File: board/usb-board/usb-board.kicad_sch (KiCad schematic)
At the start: 34 parts, among them J1 USB_C_Receptacle_USB2.0_16P, J3 RS485, J4 Conn_01x04_Pin, SW1 SW_DIP_x03, U1 AMS1117-3.3, U2 STM32F103C8T6, U3 MAX485E, Y1 8Mhz

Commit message: [ENH] Enhance scheme board
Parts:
- added R13, R14: 20, Resistor_SMD:R_1206_3216Metric_Pad1.30x1.75mm_HandSolder, symbol Device:R
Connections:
- net +3.3VA is gone; now on net +3.3V: U2.1 (VBAT), U2.24 (VDD), U2.36 (VDD), U2.48 (VDD), U2.9 (VDDA)
- net +3V3 is gone; now on net +3.3V: R12.1, U3.8 (VCC)
- net USB_D+: now also R13.1; no longer J1.A6 (D+), J1.B6 (D+)
- net USB_D-: now also R14.1; no longer J1.A7 (D-), J1.B7 (D-)
- new net: J1.A7 (D-), J1.B7 (D-), R14.2
- new net: J1.A6 (D+), J1.B6 (D+), R13.2
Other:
- moved on the sheet: R5
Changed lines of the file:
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@@
 	)
 	(junction
-		(at 213.36 86.36)
-		(diameter 0)
-		(color 0 0 0 0)
-	)
-	(junction
 		(at 240.03 147.32)
 		(diameter 0)
@@
 	)
 	(junction
+		(at 209.55 86.36)
+		(diameter 0)
+		(color 0 0 0 0)
+	)
+	(junction
 		(at 187.96 46.99)
 		(diameter 0)
@@
 	(wire
 		(pts
-			(xy 213.36 86.36) (xy 229.87 86.36)
-		)
-		(stroke
-			(width 0)
-			(type default)
-		)
-	)
-	(wire
-		(pts
 			(xy 157.48 83.82) (xy 165.1 83.82)
 		)
@@
 	(wire
 		(pts
-			(xy 213.36 86.36) (xy 198.12 86.36)
+			(xy 218.44 86.36) (xy 229.87 86.36)
 		)
 		(stroke
@@
 	(wire
 		(pts
-			(xy 213.36 82.55) (xy 213.36 86.36)
+			(xy 209.55 86.36) (xy 210.82 86.36)
+		)
+		(stroke
+			(width 0)
+			(type default)
+		)
+	)
+	(wire
+		(pts
+			(xy 209.55 82.55) (xy 209.55 86.36)
 		)
 		(stroke
@@
 	(wire
 		(pts
-			(xy 198.12 83.82) (xy 240.03 83.82)
+			(xy 198.12 83.82) (xy 219.71 83.82)
 		)
 		(stroke
@@
 	(wire
 		(pts
-			(xy 213.36 72.39) (xy 213.36 74.93)
-		)
-		(stroke
-			(width 0)
-			(type default)
-		)
-	)
-	(wire
-		(pts
 			(xy 74.93 96.52) (xy 82.55 96.52)
 		)
@@
 	(wire
 		(pts
+			(xy 227.33 83.82) (xy 240.03 83.82)
+		)
+		(stroke
+			(width 0)
+			(type default)
+		)
+	)
+	(wire
+		(pts
 			(xy 198.12 78.74) (xy 200.66 78.74)
 		)
@@
 	(wire
 		(pts
+			(xy 198.12 86.36) (xy 209.55 86.36)
+		)
+		(stroke
+			(width 0)
+			(type default)
+		)
+	)
+	(wire
+		(pts
 			(xy 60.96 39.37) (xy 60.96 41.91)
 		)
@@
 			)
 		)
-		(property "Value" "+3.3VA"
-			(at 187.96 25.4 0)
+		(property "Value" "+3.3V"
+			(at 190.5 29.2099 0)
 			(effects
 				(font
 					(size 1.27 1.27)
 				)
+				(justify left)
 			)
 		)
@@
 	)
 	(symbol
+		(lib_id "Device:R")
+		(at 223.52 83.82 90)
+		(unit 1)
+		(exclude_from_sim no)
+		(in_bom yes)
+		(on_board yes)
+		(dnp no)
+		(fields_autoplaced yes)
+		(property "Reference" "R14"
+			(at 223.52 77.47 90)
+			(effects
+				(font
+					(size 1.27 1.27)
+				)
+			)
+		)
+		(property "Value" "20"
+			(at 223.52 80.01 90)
+			(effects
+				(font
+					(size 1.27 1.27)
+				)
+			)
+		)
+		(property "Footprint" "Resistor_SMD:R_1206_3216Metric_Pad1.30x1.75mm_HandSolder"
+			(at 223.52 85.598 90)
+			(effects
+				(font
+					(size 1.27 1.27)
+				)
+				(hide yes)
+			)
+		)
+		(property "Datasheet" "~"
+			(at 223.52 83.82 0)
+			(effects
+				(font
+					(size 1.27 1.27)
+				)
+				(hide yes)
+			)
+		)
+		(property "Description" ""
+			(at 223.52 83.82 0)
+			(effects
+				(font
+					(size 1.27 1.27)
+				)
+			)
+		)
+		(pin "1"
+		)
+		(pin "2"
+		)
+		(instances
+			(project "usb-board"
+				(path "/738c6582-c171-41c5-9c7c-967a52446e9f"
+					(reference "R14")
+					(unit 1)
+				)
+			)
+		)
+	)
+	(symbol
 		(lib_id "power:GND")
 		(at 21.59 153.67 0)
@@
 		(on_board yes)
 		(dnp no)
-		(fields_autoplaced yes)
 		(property "Reference" "#PWR08"
 			(at 57.15 80.01 0)
@@
 			)
 		)
-		(property "Value" "+3V3"
-			(at 57.15 71.12 0)
+		(property "Value" "+3.3V"
+			(at 56.134 70.866 0)
 			(effects
 				(font
 					(size 1.27 1.27)
 				)
+				(justify left)
 			)
 		)
@@
 	(symbol
 		(lib_id "Device:R")
-		(at 213.36 78.74 0)
+		(at 209.55 78.74 0)
 		(unit 1)
 		(exclude_from_sim no)
@@
 		(on_board yes)
 		(dnp no)
-		(fields_autoplaced yes)
 		(property "Reference" "R5"
-			(at 215.9 77.47 0)
+			(at 212.09 77.47 0)
 			(effects
 				(font
@@
 		)
 		(property "Value" "1K5"
-			(at 215.9 80.01 0)
+			(at 212.09 80.01 0)
 			(effects
 				(font
@@
 		)
 		(property "Footprint" "Resistor_SMD:R_1206_3216Metric_Pad1.30x1.75mm_HandSolder"
-			(at 211.582 78.74 90)
+			(at 207.772 78.74 90)
 			(effects
 				(font
@@
 		)
 		(property "Datasheet" "~"
-			(at 213.36 78.74 0)
+			(at 209.55 78.74 0)
 			(effects
 				(font
@@
 		)
 		(property "Description" ""
-			(at 213.36 78.74 0)
+			(at 209.55 78.74 0)
 			(effects
 				(font
@@
 	(symbol
 		(lib_id "Device:R")
+		(at 214.63 86.36 90)
+		(unit 1)
+		(exclude_from_sim no)
+		(in_bom yes)
+		(on_board yes)
+		(dnp no)
+		(property "Reference" "R13"
+			(at 214.63 90.424 90)
+			(effects
+				(font
+					(size 1.27 1.27)
+				)
+			)
+		)
+		(property "Value" "20"
+			(at 214.376 88.646 90)
+			(effects
+				(font
+					(size 1.27 1.27)
+				)
+			)
+		)
+		(property "Footprint" "Resistor_SMD:R_1206_3216Metric_Pad1.30x1.75mm_HandSolder"
+			(at 214.63 88.138 90)
+			(effects
+				(font
+					(size 1.27 1.27)
+				)
+				(hide yes)
+			)
+		)
+		(property "Datasheet" "~"
+			(at 214.63 86.36 0)
+			(effects
+				(font
+					(size 1.27 1.27)
+				)
+				(hide yes)
+			)
+		)
+		(property "Description" ""
+			(at 214.63 86.36 0)
+			(effects
+				(font
+					(size 1.27 1.27)
+				)
+			)
+		)
+		(pin "1"
+		)
+		(pin "2"
+		)
+		(instances
+			(project "usb-board"
+				(path "/738c6582-c171-41c5-9c7c-967a52446e9f"
+					(reference "R13")
+					(unit 1)
+				)
+			)
+		)
+	)
+	(symbol
+		(lib_id "Device:R")
 		(at 73.66 148.59 180)
 		(unit 1)
@@
 			)
 		)
-		(property "Value" "+3V3"
-			(at 104.14 36.83 0)
+		(property "Value" "+3.3V"
+			(at 106.68 40.6399 0)
 			(effects
 				(font
 					(size 1.27 1.27)
 				)
+				(justify left)
 			)
 		)
@@
 	(symbol
 		(lib_id "power:+3.3V")
-		(at 213.36 72.39 0)
+		(at 209.55 74.93 0)
 		(unit 1)
 		(exclude_from_sim no)
@@
 		(fields_autoplaced yes)
 		(property "Reference" "#PWR018"
-			(at 213.36 76.2 0)
+			(at 209.55 78.74 0)
 			(effects
 				(font
@@
 		)
 		(property "Value" "+3.3V"
-			(at 213.36 67.31 0)
+			(at 209.55 69.85 0)
 			(effects
 				(font
@@
 		)
 		(property "Footprint" ""
-			(at 213.36 72.39 0)
+			(at 209.55 74.93 0)
 			(effects
 				(font
@@
 		)
 		(property "Datasheet" ""
-			(at 213.36 72.39 0)
+			(at 209.55 74.93 0)
 			(effects
 				(font
@@
 		)
 		(property "Description" ""
-			(at 213.36 72.39 0)
+			(at 209.55 74.93 0)
 			(effects
 				(font
@@
 		)
 		(property "Value" "+3.3V"
-			(at 60.96 26.67 0)
+			(at 63.5 30.4799 0)
 			(effects
 				(font
 					(size 1.27 1.27)
 				)
+				(justify left)
 			)
 		)

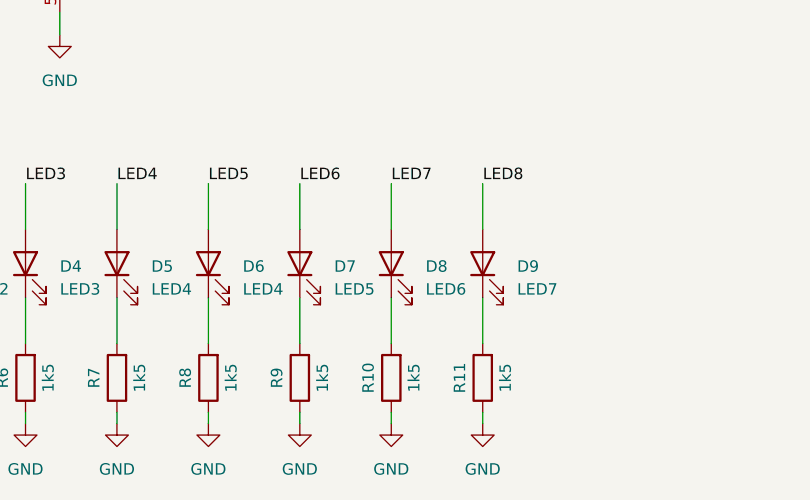
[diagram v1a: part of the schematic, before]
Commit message: [UPD] Update wrong number of leds on board
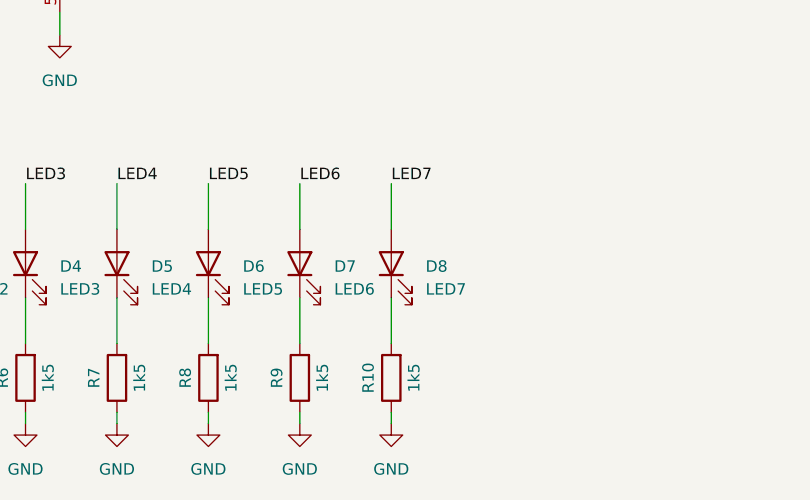
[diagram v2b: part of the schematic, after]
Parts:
- removed D9: LED7, LED_SMD:LED_1206_3216Metric_Pad1.42x1.75mm_HandSolder, symbol Device:LED
- removed R11: 1k5, Resistor_SMD:R_1206_3216Metric_Pad1.30x1.75mm_HandSolder, symbol Device:R
- D6: value LED4 -> LED5
- D7: value LED5 -> LED6
- D8: value LED6 -> LED7
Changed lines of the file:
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@@
 	(wire
 		(pts
-			(xy 104.14 152.4) (xy 104.14 153.67)
-		)
-		(stroke
-			(width 0)
-			(type default)
-		)
-	)
-	(wire
-		(pts
 			(xy 240.03 78.74) (xy 229.87 78.74)
 		)
@@
 	(wire
 		(pts
-			(xy 104.14 127) (xy 104.14 132.08)
-		)
-		(stroke
-			(width 0)
-			(type default)
-		)
-	)
-	(wire
-		(pts
 			(xy 209.55 86.36) (xy 210.82 86.36)
 		)
@@
 	(wire
 		(pts
-			(xy 104.14 139.7) (xy 104.14 144.78)
-		)
-		(stroke
-			(width 0)
-			(type default)
-		)
-	)
-	(wire
-		(pts
 			(xy 39.37 92.71) (xy 39.37 95.25)
 		)
@@
 		)
 	)
-	(label "LED8"
-		(at 104.14 127 0)
-		(effects
-			(font
-				(size 1.27 1.27)
-			)
-			(justify left bottom)
-		)
-	)
 	(label "LED"
 		(at 21.59 127 0)
@@
 	(symbol
 		(lib_id "power:GND")
-		(at 104.14 153.67 0)
-		(unit 1)
-		(exclude_from_sim no)
-		(in_bom yes)
-		(on_board yes)
-		(dnp no)
-		(fields_autoplaced yes)
-		(property "Reference" "#PWR027"
-			(at 104.14 160.02 0)
-			(effects
-				(font
-					(size 1.27 1.27)
-				)
-				(hide yes)
-			)
-		)
-		(property "Value" "GND"
-			(at 104.14 158.75 0)
-			(effects
-				(font
-					(size 1.27 1.27)
-				)
-			)
-		)
-		(property "Footprint" ""
-			(at 104.14 153.67 0)
-			(effects
-				(font
-					(size 1.27 1.27)
-				)
-				(hide yes)
-			)
-		)
-		(property "Datasheet" ""
-			(at 104.14 153.67 0)
-			(effects
-				(font
-					(size 1.27 1.27)
-				)
-				(hide yes)
-			)
-		)
-		(property "Description" ""
-			(at 104.14 153.67 0)
-			(effects
-				(font
-					(size 1.27 1.27)
-				)
-			)
-		)
-		(pin "1"
-		)
-		(instances
-			(project "usb-board"
-				(path "/738c6582-c171-41c5-9c7c-967a52446e9f"
-					(reference "#PWR027")
-					(unit 1)
-				)
-			)
-		)
-	)
-	(symbol
-		(lib_id "power:GND")
 		(at 250.19 58.42 0)
 		(unit 1)
@@
 	)
 	(symbol
-		(lib_id "Device:R")
-		(at 104.14 148.59 180)
-		(unit 1)
-		(exclude_from_sim no)
-		(in_bom yes)
-		(on_board yes)
-		(dnp no)
-		(property "Reference" "R11"
-			(at 101.6 148.59 90)
-			(effects
-				(font
-					(size 1.27 1.27)
-				)
-			)
-		)
-		(property "Value" "1k5"
-			(at 106.68 148.59 90)
-			(effects
-				(font
-					(size 1.27 1.27)
-				)
-			)
-		)
-		(property "Footprint" "Resistor_SMD:R_1206_3216Metric_Pad1.30x1.75mm_HandSolder"
-			(at 105.918 148.59 90)
-			(effects
-				(font
-					(size 1.27 1.27)
-				)
-				(hide yes)
-			)
-		)
-		(property "Datasheet" "~"
-			(at 104.14 148.59 0)
-			(effects
-				(font
-					(size 1.27 1.27)
-				)
-				(hide yes)
-			)
-		)
-		(property "Description" ""
-			(at 104.14 148.59 0)
-			(effects
-				(font
-					(size 1.27 1.27)
-				)
-			)
-		)
-		(pin "1"
-		)
-		(pin "2"
-		)
-		(instances
-			(project "usb-board"
-				(path "/738c6582-c171-41c5-9c7c-967a52446e9f"
-					(reference "R11")
-					(unit 1)
-				)
-			)
-		)
-	)
-	(symbol
 		(lib_id "Interface_UART:MAX485E")
 		(at 57.15 92.71 0)
@@
 			)
 		)
-		(property "Value" "LED5"
+		(property "Value" "LED6"
 			(at 87.63 138.7474 90)
 			(effects
@@
 			)
 		)
-		(property "Value" "LED4"
+		(property "Value" "LED5"
 			(at 77.47 138.7474 90)
 			(effects
@@
 			)
 		)
-		(property "Value" "LED6"
+		(property "Value" "LED7"
 			(at 97.79 138.7474 90)
 			(effects
@@
 					(unit 1)
 				)
-			)
-		)
-	)
-	(symbol
-		(lib_id "Device:LED")
-		(at 104.14 135.89 90)
-		(unit 1)
-		(exclude_from_sim no)
-		(in_bom yes)
-		(on_board yes)
-		(dnp no)
-		(fields_autoplaced yes)
-		(property "Reference" "D9"
-			(at 107.95 136.2074 90)
-			(effects
-				(font
-					(size 1.27 1.27)
-				)
-				(justify right)
-			)
-		)
-		(property "Value" "LED7"
-			(at 107.95 138.7474 90)
-			(effects
-				(font
-					(size 1.27 1.27)
-				)
-				(justify right)
-			)
-		)
-		(property "Footprint" "LED_SMD:LED_1206_3216Metric_Pad1.42x1.75mm_HandSolder"
-			(at 104.14 135.89 0)
-			(effects
-				(font
-					(size 1.27 1.27)
-				)
-				(hide yes)
-			)
-		)
-		(property "Datasheet" "~"
-			(at 104.14 135.89 0)
-			(effects
-				(font
-					(size 1.27 1.27)
-				)
-				(hide yes)
-			)
-		)
-		(property "Description" ""
-			(at 104.14 135.89 0)
-			(effects
-				(font
-					(size 1.27 1.27)
-				)
-			)
-		)
-		(pin "1"
-		)
-		(pin "2"
-		)
-		(instances
-			(project "usb-board"
-				(path "/738c6582-c171-41c5-9c7c-967a52446e9f"
-					(reference "D9")
-					(unit 1)
-				)
